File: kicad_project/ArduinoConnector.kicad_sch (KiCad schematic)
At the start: 9 parts, among them J5 Power, J6 Analog, J7 Digital/PWM, J8 Digital/PWM

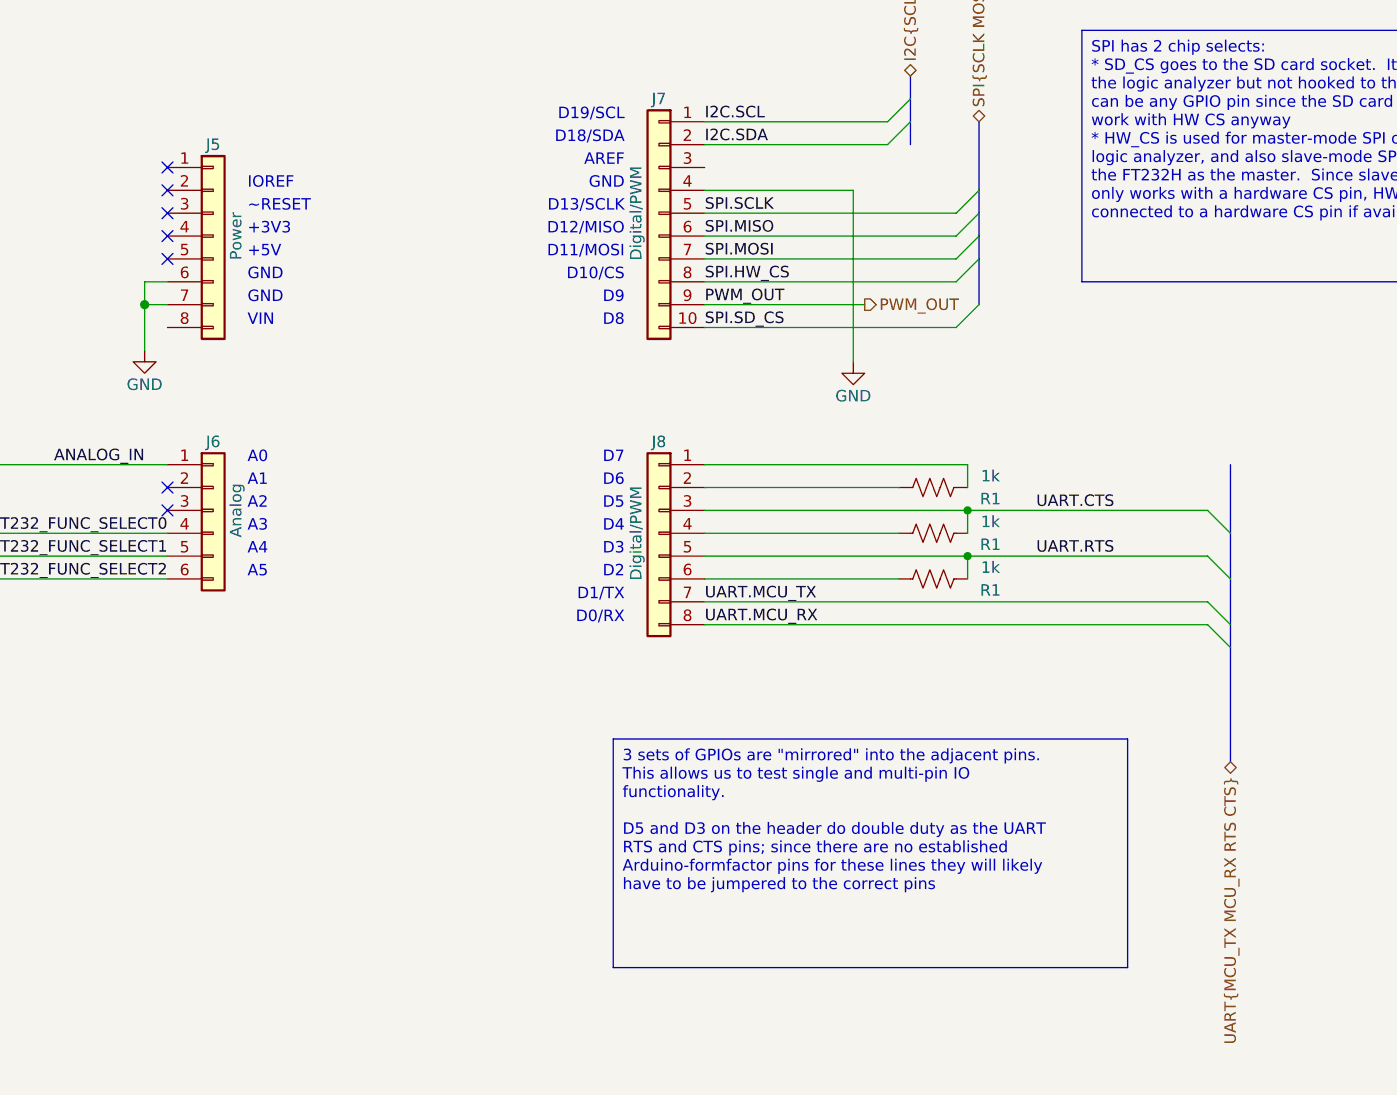
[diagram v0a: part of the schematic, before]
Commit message: Finish up initial schematic
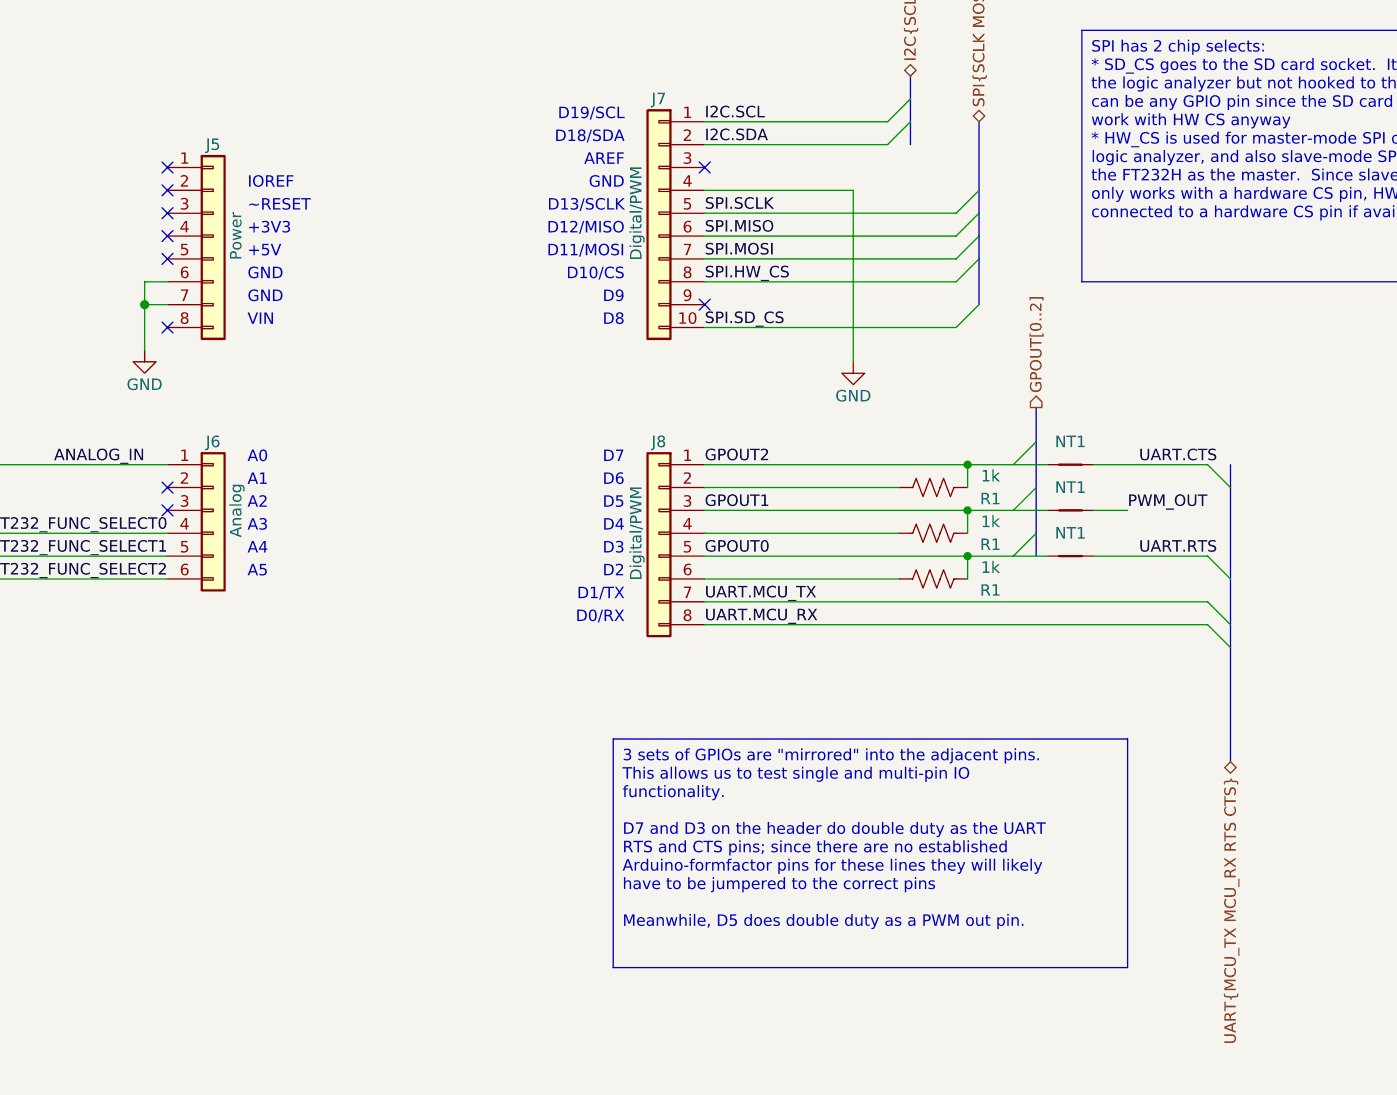
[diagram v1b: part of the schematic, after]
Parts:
- added NT1 (x3): NetTie_2, NetTie:NetTie-2_SMD_Pad0.5mm, symbol Device:NetTie_2
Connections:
- net PWM_OUT: now also NT1.2; no longer J7.9 (Pin_9)
- net UART.CTS: now also NT1.2; no longer J8.3 (Pin_3), R1.2
- net UART.RTS: now also NT1.2; no longer J8.5 (Pin_5), R1.2
- net GPOUT2: now reaches J8.1 (Pin_1), R1.2
- net GPOUT2: now also NT1.1
- new net GPOUT0: J8.5 (Pin_5), NT1.1, R1.2
- new net GPOUT1: J8.3 (Pin_3), NT1.1, R1.2
- no-connect marks 7 -> 10
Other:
- title: (none) -> Arduino Connector

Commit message: Add part numbers for capacitors, start working on BoM job
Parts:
- C9: LibRef (none) -> CL31B105KBHNNNE; Supplier (none) -> Digi-Key
- J5, J6, J7, J8, R1: Supplier (none) -> Digi-Key
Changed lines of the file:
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@@
+      (effects (font (size 1.27 1.27)) hide)
+    )
+    (property "Supplier" "Digi-Key" (at 127 102.87 0)
+      (effects (font (size 1.27 1.27)) hide)
+    )
+    (property "LibRef" "" (at 127 102.87 0)
       (effects (font (size 1.27 1.27)) hide)
     )
@@
       (effects (font (size 1.27 1.27)) hide)
     )
+    (property "LibRef" "" (at 222.25 97.79 0)
+      (effects (font (size 1.27 1.27)) hide)
+    )
     (pin "1")
     (pin "2")
@@
     )
     (property "SKU" "SAM8866-ND" (at 176.53 105.41 0)
+      (effects (font (size 1.27 1.27)) hide)
+    )
+    (property "Supplier" "Digi-Key" (at 176.53 105.41 0)
+      (effects (font (size 1.27 1.27)) hide)
+    )
+    (property "LibRef" "" (at 176.53 105.41 0)
       (effects (font (size 1.27 1.27)) hide)
     )
@@
       (effects (font (size 1.27 1.27)) hide)
     )
+    (property "Supplier" "Digi-Key" (at 82.55 97.79 0)
+      (effects (font (size 1.27 1.27)) hide)
+    )
+    (property "LibRef" "" (at 82.55 97.79 0)
+      (effects (font (size 1.27 1.27)) hide)
+    )
     (pin "1")
     (pin "2")
@@
     )
     (property "Datasheet" "~" (at 222.25 107.95 0)
+      (effects (font (size 1.27 1.27)) hide)
+    )
+    (property "LibRef" "" (at 222.25 107.95 0)
       (effects (font (size 1.27 1.27)) hide)
     )
@@
       (effects (font (size 1.27 1.27)) hide)
     )
+    (property "Supplier" "Digi-Key" (at 72.39 102.87 0)
+      (effects (font (size 1.27 1.27)) hide)
+    )
+    (property "LibRef" "CL31B105KBHNNNE" (at 72.39 102.87 0)
+      (effects (font (size 1.27 1.27)) hide)
+    )
     (pin "1")
     (pin "2")
@@
     )
     (property "Datasheet" "~" (at 207.01 105.41 0)
+      (effects (font (size 1.27 1.27)) hide)
+    )
+    (property "Supplier" "Digi-Key" (at 207.01 105.41 0)
+      (effects (font (size 1.27 1.27)) hide)
+    )
+    (property "LibRef" "" (at 207.01 105.41 0)
       (effects (font (size 1.27 1.27)) hide)
     )
@@
       (effects (font (size 1.27 1.27)) hide)
     )
+    (property "LibRef" "" (at 222.25 102.87 0)
+      (effects (font (size 1.27 1.27)) hide)
+    )
     (pin "1")
     (pin "2")
@@
     )
     (property "SKU" "SAM8866-ND" (at 127 72.39 0)
+      (effects (font (size 1.27 1.27)) hide)
+    )
+    (property "Supplier" "Digi-Key" (at 127 72.39 0)
+      (effects (font (size 1.27 1.27)) hide)
+    )
+    (property "LibRef" "" (at 127 72.39 0)
       (effects (font (size 1.27 1.27)) hide)
     )
@@
     )
     (property "SKU" "SSW-110-03-T-S-ND" (at 176.53 69.85 0)
+      (effects (font (size 1.27 1.27)) hide)
+    )
+    (property "Supplier" "Digi-Key" (at 176.53 69.85 0)
+      (effects (font (size 1.27 1.27)) hide)
+    )
+    (property "LibRef" "" (at 176.53 69.85 0)
       (effects (font (size 1.27 1.27)) hide)
     )
@@
       (effects (font (size 1.27 1.27)) hide)
     )
+    (property "Supplier" "Digi-Key" (at 207.01 110.49 0)
+      (effects (font (size 1.27 1.27)) hide)
+    )
+    (property "LibRef" "" (at 207.01 110.49 0)
+      (effects (font (size 1.27 1.27)) hide)
+    )
     (pin "1")
     (pin "2")
@@
       (effects (font (size 1.27 1.27)) hide)
     )
+    (property "Supplier" "Digi-Key" (at 207.01 100.33 0)
+      (effects (font (size 1.27 1.27)) hide)
+    )
+    (property "LibRef" "" (at 207.01 100.33 0)
+      (effects (font (size 1.27 1.27)) hide)
+    )

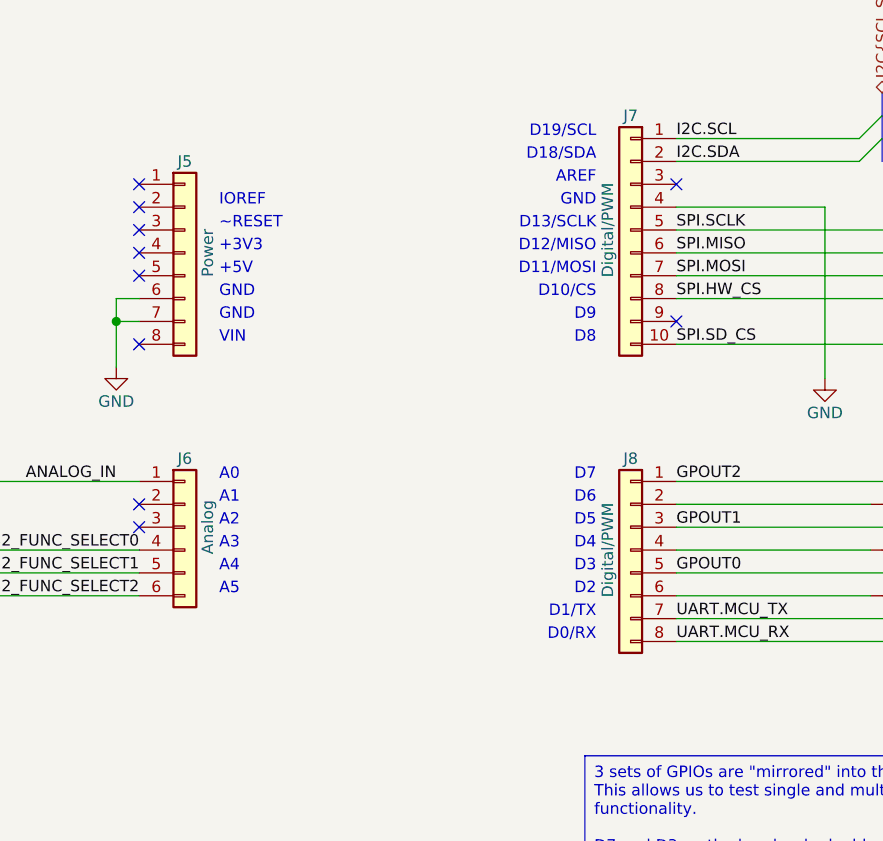
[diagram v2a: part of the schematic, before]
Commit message: Fill in all part numbers, add pcbinv bom job
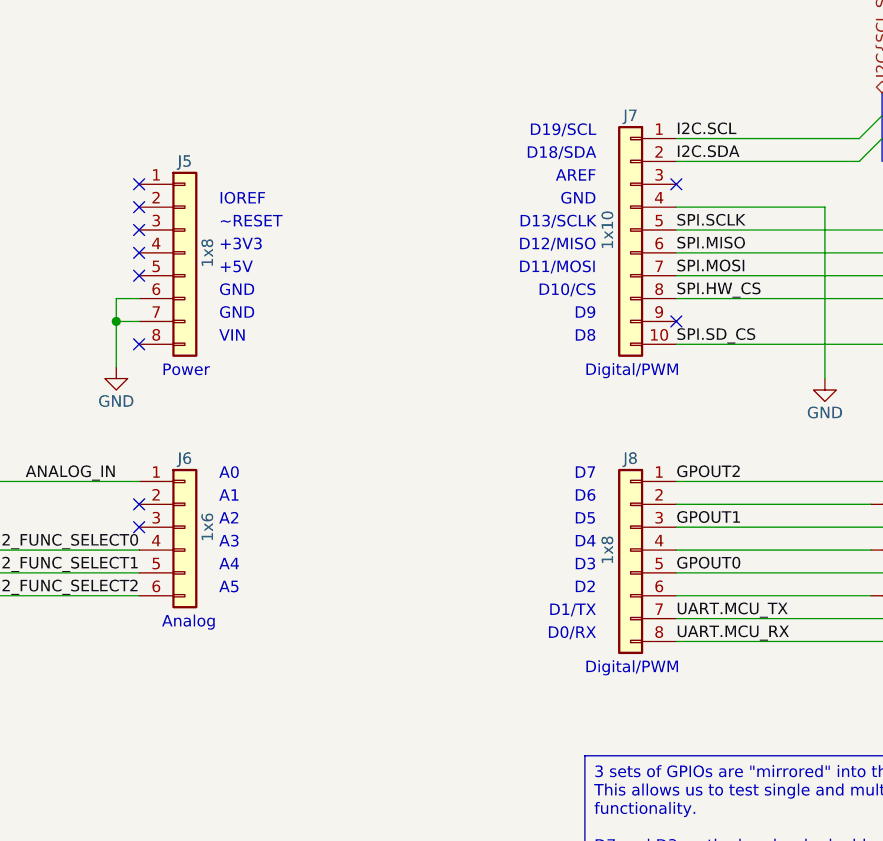
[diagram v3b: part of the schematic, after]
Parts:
- J5: value Power -> 1x8; LibRef (none) -> HEADER_8x1_LONG_TAIL
- J6: value Analog -> 1x6; LibRef (none) -> HEADER_6x1_LONG_TAIL; SKU SSW-106-03-T-S-ND -> SAM8865-ND
- J7: value Digital/PWM -> 1x10; LibRef (none) -> HEADER_10x1_LONG_TAIL
- J8: value Digital/PWM -> 1x8; LibRef (none) -> HEADER_8x1_LONG_TAIL
- R1: LibRef (none) -> RC1206FR-071K5L; SKU (none) -> 311-1.50KFRCT-ND
- R1: LibRef (none) -> P1.00KFCT-ND; SKU (none) -> ERJ-8ENF1001V
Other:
- note added: "Analog"
- note added: "Digital/PWM"
- note added: "Power"
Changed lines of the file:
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@@
     (effects (font (size 1.27 1.27)) (justify right bottom))
+  )
+  (text "Analog" (at 124.46 114.3 0)
+    (effects (font (size 1.27 1.27)) (justify left bottom))
   )
   (text "GND" (at 130.81 80.01 0)
@@
     (effects (font (size 1.27 1.27)) (justify left bottom))
   )
+  (text "Digital/PWM" (at 171.45 119.38 0)
+    (effects (font (size 1.27 1.27)) (justify left bottom))
+  )
   (text "D0/RX" (at 172.72 115.57 0)
     (effects (font (size 1.27 1.27)) (justify right bottom))
@@
     (effects (font (size 1.27 1.27)) (justify right bottom))
   )
+  (text "Power" (at 124.46 86.36 0)
+    (effects (font (size 1.27 1.27)) (justify left bottom))
+  )
   (text "A4" (at 130.81 107.95 0)
     (effects (font (size 1.27 1.27)) (justify left bottom))
@@
   (text "D8" (at 172.72 82.55 0)
     (effects (font (size 1.27 1.27)) (justify right bottom))
+  )
+  (text "Digital/PWM" (at 171.45 86.36 0)
+    (effects (font (size 1.27 1.27)) (justify left bottom))
   )
   (text "D12/MISO" (at 172.72 72.39 0)
@@
       (effects (font (size 1.27 1.27)))
     )
-    (property "Value" "Analog" (at 129.54 102.87 90)
+    (property "Value" "1x6" (at 129.54 102.87 90)
       (effects (font (size 1.27 1.27)))
     )
@@
       (effects (font (size 1.27 1.27)) hide)
     )
-    (property "SKU" "SSW-106-03-T-S-ND" (at 127 102.87 0)
+    (property "SKU" "SAM8865-ND" (at 127 102.87 0)
       (effects (font (size 1.27 1.27)) hide)
     )
@@
       (effects (font (size 1.27 1.27)) hide)
     )
-    (property "LibRef" "" (at 127 102.87 0)
+    (property "LibRef" "HEADER_6x1_LONG_TAIL" (at 127 102.87 0)
+      (effects (font (size 1.27 1.27)) hide)
+    )
+    (property "Description" "Female Pin Header 0.1\" 6 Pin 10mm Leads" (at 127 102.87 0)
       (effects (font (size 1.27 1.27)) hide)
     )
@@
       (effects (font (size 1.27 1.27)))
     )
-    (property "Value" "Digital/PWM" (at 173.99 105.41 90)
+    (property "Value" "1x8" (at 173.99 105.41 90)
       (effects (font (size 1.27 1.27)))
     )
@@
       (effects (font (size 1.27 1.27)) hide)
     )
-    (property "LibRef" "" (at 176.53 105.41 0)
+    (property "LibRef" "HEADER_8x1_LONG_TAIL" (at 176.53 105.41 0)
+      (effects (font (size 1.27 1.27)) hide)
+    )
+    (property "Description" "Female Pin Header 0.1\" 8 Pin 10mm Leads" (at 176.53 105.41 0)
       (effects (font (size 1.27 1.27)) hide)
     )
@@
       (effects (font (size 1.27 1.27)) hide)
     )
-    (property "LibRef" "" (at 82.55 97.79 0)
+    (property "LibRef" "RC1206FR-071K5L" (at 82.55 97.79 0)
+      (effects (font (size 1.27 1.27)) hide)
+    )
+    (property "Description" "RES 1.5k Ohm 1% 1/4W 1206" (at 82.55 97.79 0)
+      (effects (font (size 1.27 1.27)) hide)
+    )
+    (property "SKU" "311-1.50KFRCT-ND" (at 82.55 97.79 0)
       (effects (font (size 1.27 1.27)) hide)
     )
@@
       (effects (font (size 1.27 1.27)) hide)
     )
-    (property "LibRef" "" (at 207.01 105.41 0)
+    (property "LibRef" "P1.00KFCT-ND" (at 207.01 105.41 0)
+      (effects (font (size 1.27 1.27)) hide)
+    )
+    (property "SKU" "ERJ-8ENF1001V" (at 207.01 105.41 0)
       (effects (font (size 1.27 1.27)) hide)
     )
@@
       (effects (font (size 1.27 1.27)))
     )
-    (property "Value" "Power" (at 129.54 72.39 90)
+    (property "Value" "1x8" (at 129.54 72.39 90)
       (effects (font (size 1.27 1.27)))
     )
@@
       (effects (font (size 1.27 1.27)) hide)
     )
-    (property "LibRef" "" (at 127 72.39 0)
+    (property "LibRef" "HEADER_8x1_LONG_TAIL" (at 127 72.39 0)
+      (effects (font (size 1.27 1.27)) hide)
+    )
+    (property "Description" "Female Pin Header 0.1\" 8 Pin 10mm Leads" (at 127 72.39 0)
       (effects (font (size 1.27 1.27)) hide)
     )
@@
       (effects (font (size 1.27 1.27)))
     )
-    (property "Value" "Digital/PWM" (at 173.99 69.85 90)
+    (property "Value" "1x10" (at 173.99 69.85 90)
       (effects (font (size 1.27 1.27)))
     )
@@
       (effects (font (size 1.27 1.27)) hide)
     )
-    (property "LibRef" "" (at 176.53 69.85 0)
+    (property "LibRef" "HEADER_10x1_LONG_TAIL" (at 176.53 69.85 0)
+      (effects (font (size 1.27 1.27)) hide)
+    )
+    (property "Description" "Female Pin Header 0.1\" 10 Pin 10mm Leads" (at 176.53 69.85 0)
       (effects (font (size 1.27 1.27)) hide)
     )
@@
       (effects (font (size 1.27 1.27)) hide)
     )
-    (property "LibRef" "" (at 207.01 110.49 0)
+    (property "LibRef" "P1.00KFCT-ND" (at 207.01 110.49 0)
+      (effects (font (size 1.27 1.27)) hide)
+    )
+    (property "SKU" "ERJ-8ENF1001V" (at 207.01 110.49 0)
       (effects (font (size 1.27 1.27)) hide)
     )
@@
       (effects (font (size 1.27 1.27)) hide)
     )
-    (property "LibRef" "" (at 207.01 100.33 0)
-      (effects (font (size 1.27 1.27)) hide)
-    )
+    (property "LibRef" "P1.00KFCT-ND" (at 207.01 100.33 0)
+      (effects (font (size 1.27 1.27)) hide)
+    )
+    (property "SKU" "ERJ-8ENF1001V" (at 207.01 100.33 0)
+      (effects (font (size 1.27 1.27)) hide)
+    )

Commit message: Finish assigning schematic part numbers
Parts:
- R1: LibRef P1.00KFCT-ND -> ERJ-8ENF1001V; SKU ERJ-8ENF1001V -> P1.00KFCT-ND
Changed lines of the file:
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@@
       (effects (font (size 1.27 1.27)) hide)
     )
-    (property "LibRef" "P1.00KFCT-ND" (at 207.01 105.41 0)
-      (effects (font (size 1.27 1.27)) hide)
-    )
-    (property "SKU" "ERJ-8ENF1001V" (at 207.01 105.41 0)
+    (property "LibRef" "ERJ-8ENF1001V" (at 207.01 105.41 0)
+      (effects (font (size 1.27 1.27)) hide)
+    )
+    (property "SKU" "P1.00KFCT-ND" (at 207.01 105.41 0)
       (effects (font (size 1.27 1.27)) hide)
     )
@@
       (effects (font (size 1.27 1.27)) hide)
     )
-    (property "LibRef" "P1.00KFCT-ND" (at 207.01 110.49 0)
-      (effects (font (size 1.27 1.27)) hide)
-    )
-    (property "SKU" "ERJ-8ENF1001V" (at 207.01 110.49 0)
+    (property "LibRef" "ERJ-8ENF1001V" (at 207.01 110.49 0)
+      (effects (font (size 1.27 1.27)) hide)
+    )
+    (property "SKU" "P1.00KFCT-ND" (at 207.01 110.49 0)
       (effects (font (size 1.27 1.27)) hide)
     )
@@
       (effects (font (size 1.27 1.27)) hide)
     )
-    (property "LibRef" "P1.00KFCT-ND" (at 207.01 100.33 0)
-      (effects (font (size 1.27 1.27)) hide)
-    )
-    (property "SKU" "ERJ-8ENF1001V" (at 207.01 100.33 0)
-      (effects (font (size 1.27 1.27)) hide)
-    )
+    (property "LibRef" "ERJ-8ENF1001V" (at 207.01 100.33 0)
+      (effects (font (size 1.27 1.27)) hide)
+    )
+    (property "SKU" "P1.00KFCT-ND" (at 207.01 100.33 0)
+      (effects (font (size 1.27 1.27)) hide)
+    )
